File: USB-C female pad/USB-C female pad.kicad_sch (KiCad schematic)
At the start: 5 parts, among them J1 USB_C_Receptacle_PowerOnly_6P, J2 Conn_01x02_Socket

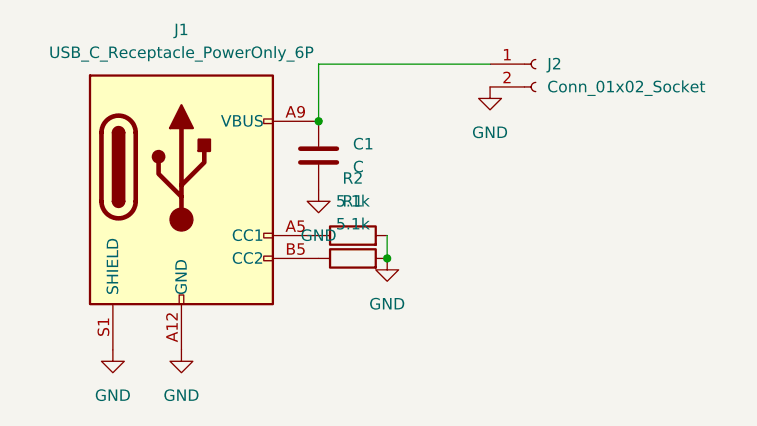
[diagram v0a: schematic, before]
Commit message: Small trace changes
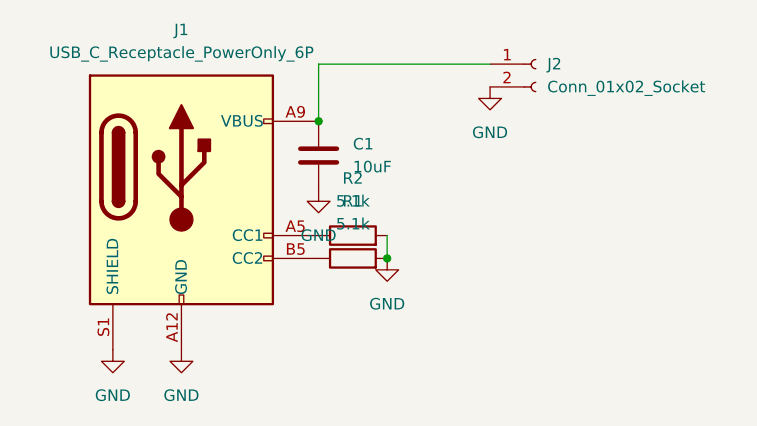
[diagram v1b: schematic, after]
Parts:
- C1: value C -> 10uF; footprint (none) -> Capacitor_SMD:C_0805_2012Metric_Pad1.18x1.45mm_HandSolder
- J2: footprint (none) -> Connector_PinHeader_2.54mm:PinHeader_1x02_P2.54mm_Vertical
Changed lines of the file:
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@@
 			)
 		)
-		(property "Footprint" ""
+		(property "Footprint" "Connector_PinHeader_2.54mm:PinHeader_1x02_P2.54mm_Vertical"
 			(at 130.81 62.23 0)
 			(effects
@@
 			)
 		)
-		(property "Value" "C"
+		(property "Value" "10uF"
 			(at 110.49 73.6599 0)
 			(effects
@@
 			)
 		)
-		(property "Footprint" ""
+		(property "Footprint" "Capacitor_SMD:C_0805_2012Metric_Pad1.18x1.45mm_HandSolder"
 			(at 107.6452 76.2 0)
 			(effects

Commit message: Add SP0503BAHTG to USB-C pad
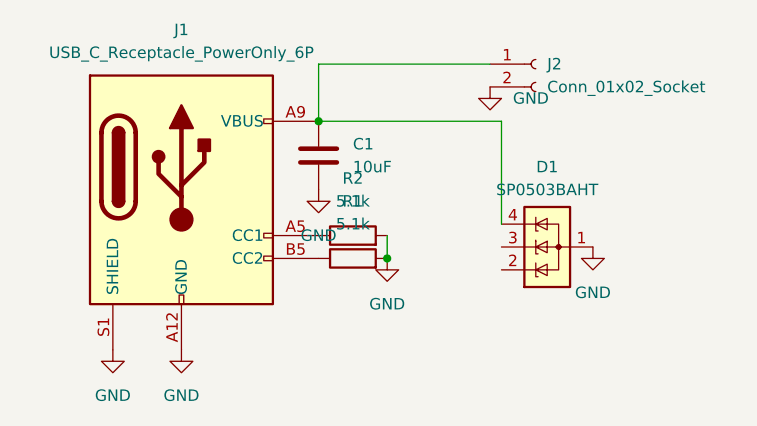
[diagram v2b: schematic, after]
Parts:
- added D1: SP0503BAHT, Package_TO_SOT_SMD:SOT-143, symbol Power_Protection:SP0503BAHT
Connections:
- net GND: now also D1.1 (A)
- net at C1.1, J1.A9 (VBUS), J1.B9 (VBUS)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: now also D1.4 (K)
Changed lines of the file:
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@@
+	(wire
+		(pts
+			(xy 127 68.58) (xy 106.68 68.58)
+		)
+		(stroke
+			(width 0)
+			(type default)
+		)
+	)
+	(wire
+		(pts
+			(xy 127 80.01) (xy 127 68.58)
+		)
+		(stroke
+			(width 0)
+			(type default)
+		)
+	)
 	(wire
 		(pts
@@
 	)
 	(symbol
+		(lib_id "Power_Protection:SP0503BAHT")
+		(at 132.08 82.55 90)
+		(unit 1)
+		(exclude_from_sim no)
+		(in_bom yes)
+		(on_board yes)
+		(dnp no)
+		(fields_autoplaced yes)
+		(property "Reference" "D1"
+			(at 132.08 73.66 90)
+			(effects
+				(font
+					(size 1.27 1.27)
+				)
+			)
+		)
+		(property "Value" "SP0503BAHT"
+			(at 132.08 76.2 90)
+			(effects
+				(font
+					(size 1.27 1.27)
+				)
+			)
+		)
+		(property "Footprint" "Package_TO_SOT_SMD:SOT-143"
+			(at 133.35 76.835 0)
+			(effects
+				(font
+					(size 1.27 1.27)
+				)
+				(justify left)
+				(hide yes)
+			)
+		)
+		(property "Datasheet" "http://www.littelfuse.com/~/media/files/littelfuse/technical%20resources/documents/data%20sheets/sp05xxba.pdf"
+			(at 128.905 79.375 0)
+			(effects
+				(font
+					(size 1.27 1.27)
+				)
+				(hide yes)
+			)
+		)
+		(property "Description" "TVS Diode Array, 5.5V Standoff, 3 Channels, SOT-143 package"
+			(at 132.08 82.55 0)
+			(effects
+				(font
+					(size 1.27 1.27)
+				)
+				(hide yes)
+			)
+		)
+		(pin "1"
+		)
+		(pin "2"
+		)
+		(pin "3"
+		)
+		(pin "4"
+		)
+		(instances
+			(project ""
+				(path "/f838683b-2a73-462a-8b53-03d83e8689c5"
+					(reference "D1")
+					(unit 1)
+				)
+			)
+		)
+	)
+	(symbol
 		(lib_id "Connector:Conn_01x02_Socket")
 		(at 130.81 62.23 0)
@@
 		)
 		(property "Value" "GND"
-			(at 125.73 69.85 0)
-			(effects
-				(font
-					(size 1.27 1.27)
-				)
+			(at 128.27 66.0399 0)
+			(effects
+				(font
+					(size 1.27 1.27)
+				)
+				(justify left)
 			)
 		)
@@
 					(unit 1)
 				)
+			)
+		)
+	)
+	(symbol
+		(lib_id "power:GND")
+		(at 137.16 82.55 0)
+		(mirror y)
+		(unit 1)
+		(exclude_from_sim no)
+		(in_bom yes)
+		(on_board yes)
+		(dnp no)
+		(property "Reference" "#PWR06"
+			(at 137.16 88.9 0)
+			(effects
+				(font
+					(size 1.27 1.27)
+				)
+				(hide yes)
+			)
+		)
+		(property "Value" "GND"
+			(at 137.16 87.63 0)
+			(effects
+				(font
+					(size 1.27 1.27)
+				)
+			)
+		)
+		(property "Footprint" ""
+			(at 137.16 82.55 0)
+			(effects
+				(font
+					(size 1.27 1.27)
+				)
+				(hide yes)
+			)
+		)
+		(property "Datasheet" ""
+			(at 137.16 82.55 0)
+			(effects
+				(font
+					(size 1.27 1.27)
+				)
+				(hide yes)
+			)
+		)
+		(property "Description" "Power symbol creates a global label with name \"GND\" , ground"
+			(at 137.16 82.55 0)
+			(effects
+				(font
+					(size 1.27 1.27)
+				)
+				(hide yes)
+			)
+		)
+		(pin "1"
+		)
+		(instances
+			(project ""
+				(path "/f838683b-2a73-462a-8b53-03d83e8689c5"
+					(reference "#PWR06")
+					(unit 1)
+				)
